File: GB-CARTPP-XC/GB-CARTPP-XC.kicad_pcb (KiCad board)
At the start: 2 copper layers, 80 x 55 mm, 29 parts, among them J1 TYPE-C-31-M-12, J2 DNP, J3 GameBoy_Cartridge_MountingPin, U1 SY6288AAAC, U2 PIC18F45K50_QFP

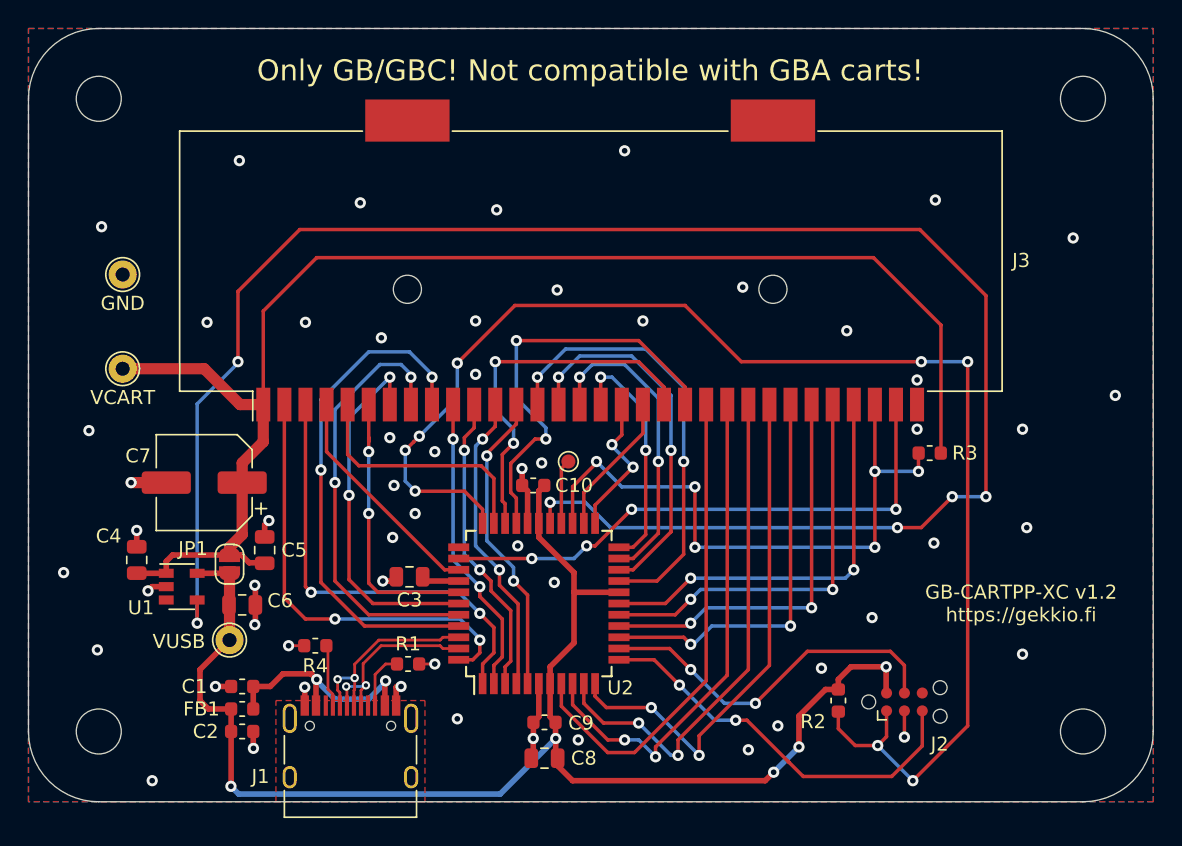
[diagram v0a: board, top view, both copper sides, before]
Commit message: Upgrade most projects to KiCad 6
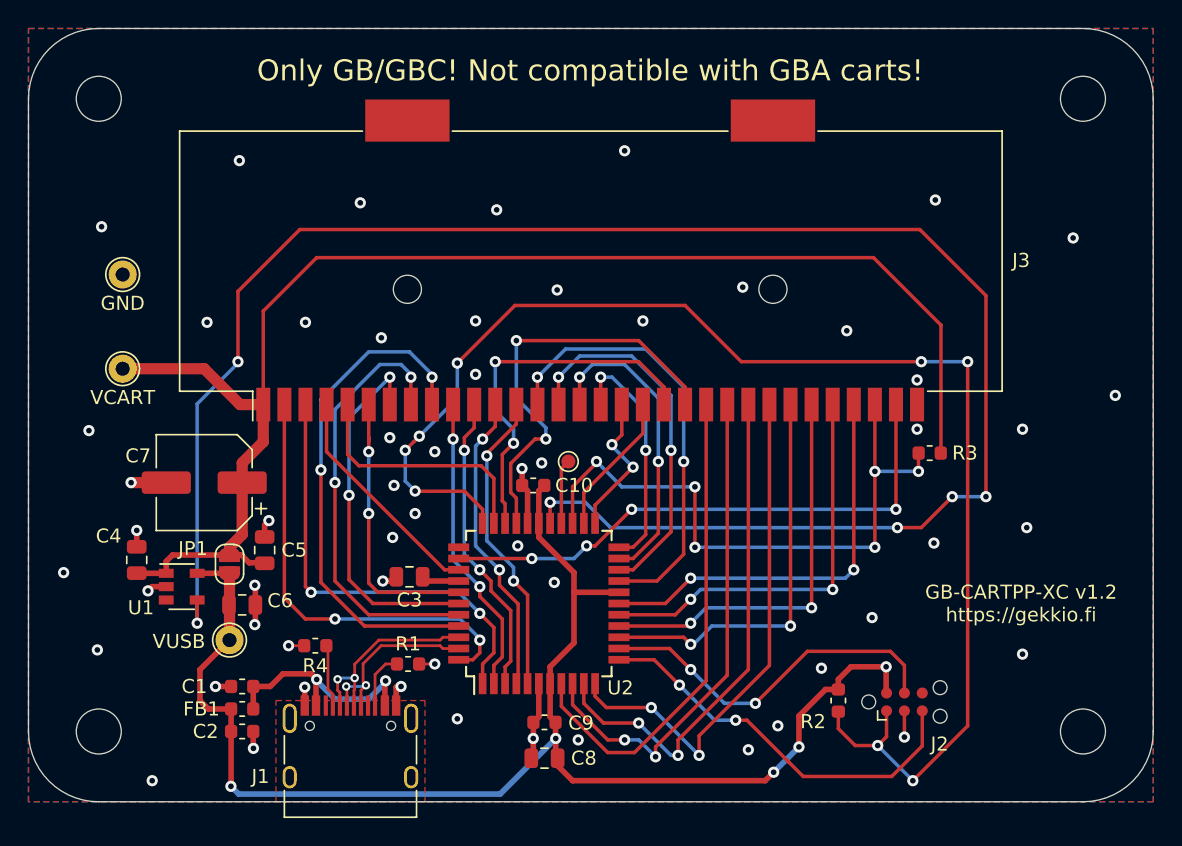
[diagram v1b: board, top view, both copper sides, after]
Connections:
- net /~CS renamed /~{CS}
- net /~P31 renamed /~{P31}
- net /~RD renamed /~{RD}
- net /~RES renamed /~{RES}
- net /~WR renamed /~{WR}
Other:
- net class Default removed
